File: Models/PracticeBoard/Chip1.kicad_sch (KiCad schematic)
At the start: 1 part, among them U1 XMC1100

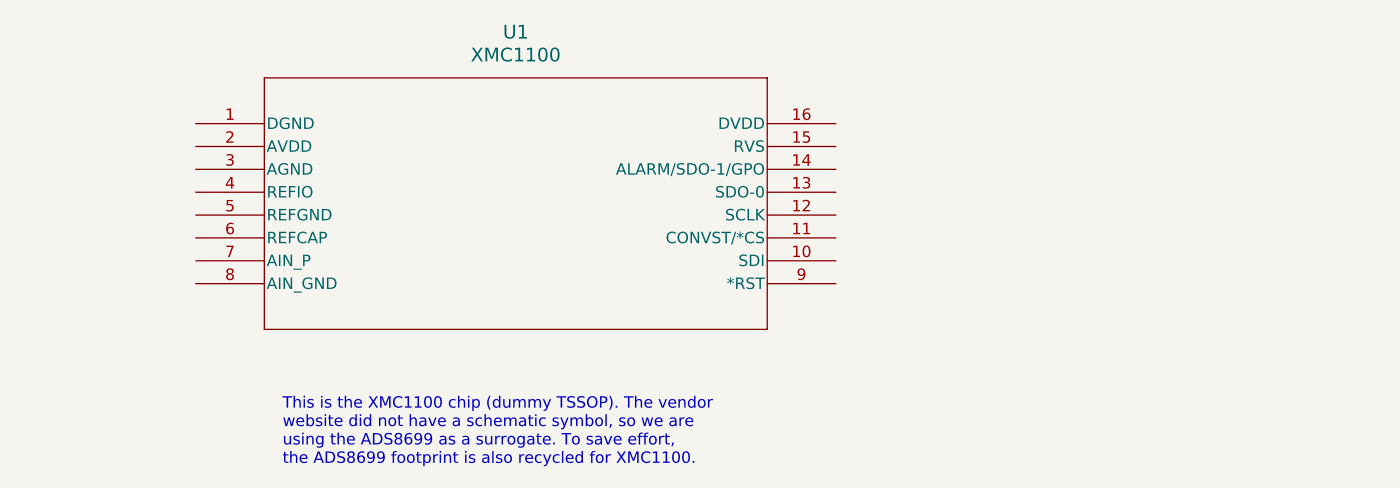
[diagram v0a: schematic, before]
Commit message: Going to practice laying out the resistors near a chip, although the annotations will likely be overwritten later, requiring a duplication of the work for PCB layout
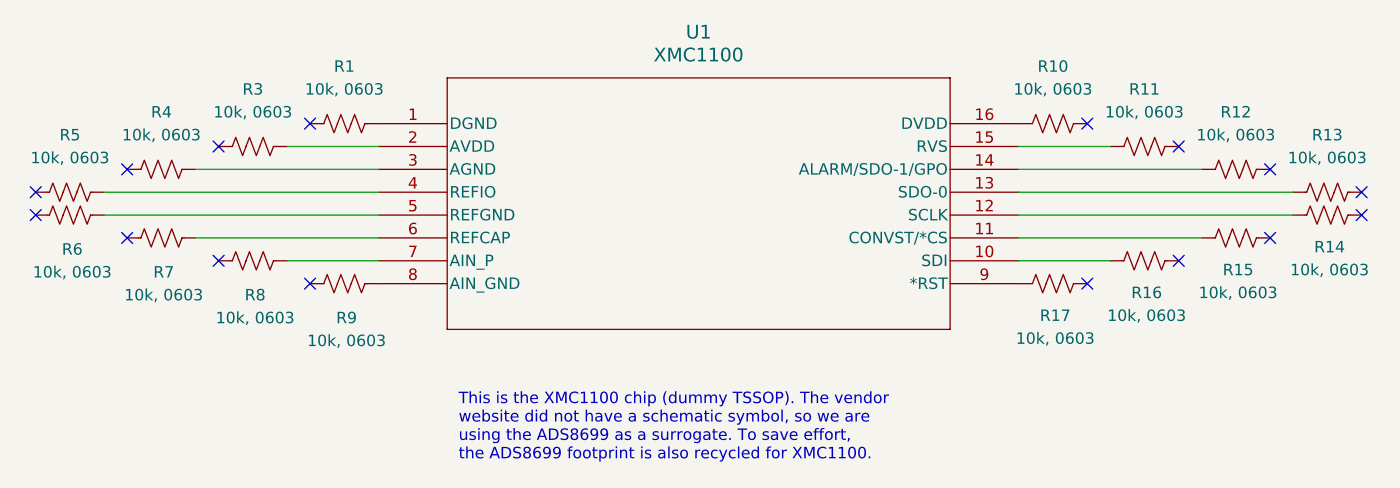
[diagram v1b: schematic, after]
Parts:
- added R1, R10, R11, R12, R13, R14, R15, R16, R17, R3, R4, R5, R6, R7, R8, R9: 10k, 0603, symbol Device:R_US
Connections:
- net at U1.1 (DGND): now also R1.2
- net at U1.10 (SDI): now also R16.1
- net at U1.11 (CONVST/*CS): now also R15.1
- net at U1.12 (SCLK): now also R14.1
- net at U1.13 (SDO-0): now also R13.1
- net at U1.14 (ALARM/SDO-1/GPO): now also R12.1
- net at U1.15 (RVS): now also R11.1
- net at U1.16 (DVDD): now also R10.1
- net at U1.2 (AVDD): now also R3.2
- net at U1.3 (AGND): now also R4.2
- net at U1.4 (REFIO): now also R5.2
- net at U1.5 (REFGND): now also R6.2
- net at U1.6 (REFCAP): now also R7.2
- net at U1.7 (AIN_P): now also R8.2
- net at U1.8 (AIN_GND): now also R9.2
- net at U1.9 (*RST): now also R17.1
- no-connect marks 0 -> 16
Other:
- moved on the sheet: U1

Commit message: Rough sketch of the layout resulted in a calculated price of
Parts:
- R1, R10, R11, R12, R13, R14, R15, R16, R17, R3, R4, R5, R6, R7, R8, R9: footprint (none) -> TwoTerminal:RESC0603
- U1: footprint (none) -> IC:ADS8699
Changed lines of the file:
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@@
 			)
 		)
-		(property "Footprint" ""
+		(property "Footprint" "TwoTerminal:RESC0603"
 			(at 100.584 95.504 90)
 			(effects
@@
 			)
 		)
-		(property "Footprint" ""
+		(property "Footprint" "TwoTerminal:RESC0603"
 			(at 209.804 85.344 90)
 			(effects
@@
 			)
 		)
-		(property "Footprint" ""
+		(property "Footprint" "TwoTerminal:RESC0603"
 			(at 189.484 80.264 90)
 			(effects
@@
 			)
 		)
-		(property "Footprint" ""
+		(property "Footprint" "TwoTerminal:RESC0603"
 			(at 219.964 87.884 90)
 			(effects
@@
 			)
 		)
-		(property "Footprint" ""
+		(property "Footprint" "TwoTerminal:RESC0603"
 			(at 189.484 98.044 90)
 			(effects
@@
 			)
 		)
-		(property "Footprint" ""
+		(property "Footprint" "TwoTerminal:RESC0603"
 			(at 90.424 85.344 90)
 			(effects
@@
 			)
 		)
-		(property "Footprint" ""
+		(property "Footprint" "TwoTerminal:RESC0603"
 			(at 100.584 82.804 90)
 			(effects
@@
 			)
 		)
-		(property "Footprint" ""
+		(property "Footprint" "TwoTerminal:RESC0603"
 			(at 199.644 82.804 90)
 			(effects
@@
 			)
 		)
-		(property "Footprint" ""
+		(property "Footprint" "TwoTerminal:RESC0603"
 			(at 199.644 95.504 90)
 			(effects
@@
 			)
 		)
-		(property "Footprint" ""
+		(property "Footprint" "TwoTerminal:RESC0603"
 			(at 219.964 90.424 90)
 			(effects
@@
 			)
 		)
-		(property "Footprint" ""
+		(property "Footprint" "TwoTerminal:RESC0603"
 			(at 110.744 98.044 90)
 			(effects
@@
 			)
 		)
-		(property "Footprint" ""
+		(property "Footprint" "TwoTerminal:RESC0603"
 			(at 90.424 92.964 90)
 			(effects
@@
 			)
 		)
-		(property "Footprint" ""
+		(property "Footprint" "IC:ADS8699"
 			(at 114.3 81.28 0)
 			(effects
@@
 			)
 		)
-		(property "Footprint" ""
+		(property "Footprint" "TwoTerminal:RESC0603"
 			(at 80.264 90.424 90)
 			(effects
@@
 			)
 		)
-		(property "Footprint" ""
+		(property "Footprint" "TwoTerminal:RESC0603"
 			(at 209.804 92.964 90)
 			(effects
@@
 			)
 		)
-		(property "Footprint" ""
+		(property "Footprint" "TwoTerminal:RESC0603"
 			(at 80.264 87.884 90)
 			(effects
@@
 			)
 		)
-		(property "Footprint" ""
+		(property "Footprint" "TwoTerminal:RESC0603"
 			(at 110.744 80.264 90)
 			(effects
